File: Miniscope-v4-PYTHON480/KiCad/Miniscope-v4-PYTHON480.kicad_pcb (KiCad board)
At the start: 6 copper layers, 10.5 x 9 mm, 32 parts, among them J1 Conn_01x20, J2 Conn_01x14, Q1 MMBT3904LP-7B, U1 LMV321IDCKR, U2 NOIP1SN0480A, U3 SiT_2.5mmx2mm

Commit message: Not sure why these files changed. Should be just minor stuff
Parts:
- moved L1 0.28 mm to (41.9, 29.4)
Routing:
- net /DOUT5: track 3.86 -> 4.43 mm
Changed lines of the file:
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@@
     (thickness 0.7874)
     (drawings 4)
-    (tracks 429)
+    (tracks 431)
     (zones 0)
     (modules 32)
@@
   )
   (module .Inductor:L_0603_1608Metric_L (layer F.Cu)
-    (at 42.133 29.436 180)
+    (at 41.8536 29.436 180)
     (descr "Inductor, Chip; 1.60 mm L X 0.80 mm W X 1.00 mm H body")
     (attr smd)
@@
   (segment (start 36.1132 28.293) (end 35.569999 28.836201) (width 0.3048) (layer B.Cu) (net 3))
   (via (at 34.9194 31.468) (size 0.3556) (drill 0.1016) (layers F.Cu B.Cu) (net 4))
-  (segment (start 39.4836 30.5884) (end 39.744299 30.327701) (width 0.0762) (layer B.Cu) (net 4))
-  (via (at 39.6946 29.69) (size 0.3556) (drill 0.1016) (layers F.Cu B.Cu) (net 4))
-  (segment (start 39.744299 30.327701) (end 39.744299 29.739699) (width 0.0762) (layer B.Cu) (net 4))
-  (segment (start 39.744299 29.739699) (end 39.6946 29.69) (width 0.0762) (layer B.Cu) (net 4))
-  (segment (start 39.509 29.8756) (end 39.509 30.562) (width 0.0762) (layer F.Cu) (net 4))
-  (segment (start 39.6946 29.69) (end 39.509 29.8756) (width 0.0762) (layer F.Cu) (net 4))
   (segment (start 40.99 29.3598) (end 41.0916 29.436) (width 0.0762) (layer F.Cu) (net 4))
   (via (at 36.570374 31.595) (size 0.3556) (drill 0.1016) (layers F.Cu B.Cu) (net 4))
@@
   (segment (start 36.8708 31.1194) (end 36.570374 31.419826) (width 0.0762) (layer F.Cu) (net 4))
   (segment (start 36.8708 31.1044) (end 36.8708 31.1194) (width 0.0762) (layer F.Cu) (net 4))
-  (segment (start 39.6946 29.438553) (end 39.6946 29.69) (width 0.3048) (layer F.Cu) (net 4))
-  (segment (start 39.951152 29.182001) (end 39.6946 29.438553) (width 0.3048) (layer F.Cu) (net 4))
-  (segment (start 40.812201 29.182001) (end 39.951152 29.182001) (width 0.3048) (layer F.Cu) (net 4))
-  (segment (start 40.99 29.3598) (end 40.812201 29.182001) (width 0.3048) (layer F.Cu) (net 4))
-  (segment (start 36.595786 31.569588) (end 36.570374 31.595) (width 0.3048) (layer In3.Cu) (net 4))
-  (segment (start 36.595786 31.399927) (end 36.595786 31.569588) (width 0.3048) (layer In3.Cu) (net 4))
-  (segment (start 39.6692 29.69) (end 39.643801 29.715399) (width 0.3048) (layer In3.Cu) (net 4))
-  (segment (start 39.6946 29.69) (end 39.6692 29.69) (width 0.3048) (layer In3.Cu) (net 4))
-  (segment (start 39.643801 29.715399) (end 39.643801 29.910473) (width 0.3048) (layer In3.Cu) (net 4))
-  (segment (start 39.643801 29.910473) (end 38.365675 31.188599) (width 0.3048) (layer In3.Cu) (net 4))
-  (segment (start 38.365675 31.188599) (end 36.807114 31.188599) (width 0.3048) (layer In3.Cu) (net 4))
-  (segment (start 36.807114 31.188599) (end 36.595786 31.399927) (width 0.3048) (layer In3.Cu) (net 4))
   (via (at 41.0916 29.436) (size 0.3556) (drill 0.1016) (layers F.Cu B.Cu) (net 4))
   (segment (start 41.244299 29.588699) (end 41.0916 29.436) (width 0.0762) (layer B.Cu) (net 4))
@@
   (segment (start 36.570374 31.595) (end 36.570374 31.7139) (width 0.3048) (layer In3.Cu) (net 4))
   (segment (start 36.570374 31.7139) (end 36.282873 32.001401) (width 0.3048) (layer In3.Cu) (net 4))
+  (via (at 39.69149 29.69) (size 0.3556) (drill 0.1016) (layers F.Cu B.Cu) (net 4))
+  (segment (start 39.509 29.87249) (end 39.513691 29.867799) (width 0.0762) (layer F.Cu) (net 4))
+  (segment (start 36.570374 31.343553) (end 36.725328 31.188599) (width 0.3048) (layer In3.Cu) (net 4))
+  (segment (start 39.4836 30.5884) (end 39.744299 30.327701) (width 0.0762) (layer B.Cu) (net 4))
+  (segment (start 39.744299 30.327701) (end 39.744299 29.994256) (width 0.0762) (layer B.Cu) (net 4))
+  (segment (start 39.69149 29.941447) (end 39.69149 29.69) (width 0.0762) (layer B.Cu) (net 4))
+  (segment (start 36.725328 31.188599) (end 38.444338 31.188599) (width 0.3048) (layer In3.Cu) (net 4))
+  (segment (start 38.444338 31.188599) (end 39.69149 29.941447) (width 0.3048) (layer In3.Cu) (net 4))
+  (segment (start 39.513691 29.867799) (end 39.69149 29.69) (width 0.0762) (layer F.Cu) (net 4))
+  (segment (start 39.744299 29.994256) (end 39.69149 29.941447) (width 0.0762) (layer B.Cu) (net 4))
+  (segment (start 36.570374 31.595) (end 36.570374 31.343553) (width 0.3048) (layer In3.Cu) (net 4))
+  (segment (start 39.509 30.562) (end 39.509 29.87249) (width 0.0762) (layer F.Cu) (net 4))
+  (segment (start 39.69149 29.941447) (end 39.69149 29.69) (width 0.3048) (layer In3.Cu) (net 4))
+  (segment (start 40.5328 28.9026) (end 39.960918 28.9026) (width 0.3048) (layer F.Cu) (net 4))
+  (segment (start 39.682076 29.680586) (end 39.69149 29.69) (width 0.3048) (layer F.Cu) (net 4))
+  (segment (start 40.99 29.3598) (end 40.5328 28.9026) (width 0.3048) (layer F.Cu) (net 4))
+  (segment (start 39.960918 28.9026) (end 39.682076 29.181442) (width 0.3048) (layer F.Cu) (net 4))
+  (segment (start 39.682076 29.181442) (end 39.682076 29.680586) (width 0.3048) (layer F.Cu) (net 4))
   (via (at 35.0464 30.7822) (size 0.3556) (drill 0.1016) (layers F.Cu B.Cu) (net 5))
   (via (at 44.2158 30.8076) (size 0.3556) (drill 0.1016) (layers F.Cu B.Cu) (net 5))
@@
   (segment (start 39.4836 30.0884) (end 39.244299 30.327701) (width 0.0762) (layer B.Cu) (net 41))
   (segment (start 39.244299 30.327701) (end 39.244299 31.308701) (width 0.0762) (layer B.Cu) (net 41))
-  (via (at 40.1772 29.6646) (size 0.3556) (drill 0.1016) (layers F.Cu B.Cu) (net 42))
-  (segment (start 39.9836 30.0884) (end 39.9836 29.8582) (width 0.0762) (layer B.Cu) (net 42))
-  (segment (start 39.9836 29.8582) (end 40.1772 29.6646) (width 0.0762) (layer B.Cu) (net 42))
-  (segment (start 40.1772 29.6646) (end 40.1772 33.0174) (width 0.0762) (layer F.Cu) (net 42))
+  (segment (start 40.088478 32.928678) (end 40.088478 29.627963) (width 0.0762) (layer F.Cu) (net 42))
+  (via (at 40.088478 29.376516) (size 0.3556) (drill 0.1016) (layers F.Cu B.Cu) (net 42))
+  (segment (start 39.9836 29.481394) (end 40.088478 29.376516) (width 0.0762) (layer B.Cu) (net 42))
+  (segment (start 40.088478 29.627963) (end 40.088478 29.376516) (width 0.0762) (layer F.Cu) (net 42))
+  (segment (start 39.9836 30.0884) (end 39.9836 29.481394) (width 0.0762) (layer B.Cu) (net 42))
+  (segment (start 40.1772 33.0174) (end 40.088478 32.928678) (width 0.0762) (layer F.Cu) (net 42))
   (via (at 41.625 32.40781) (size 0.3556) (drill 0.1016) (layers F.Cu B.Cu) (net 43))
   (segment (start 41.625 32.130953) (end 41.625 32.156363) (width 0.0762) (layer B.Cu) (net 43))
@@
   (segment (start 40.4836 30.0884) (end 40.744299 30.349099) (width 0.0762) (layer B.Cu) (net 43))
   (segment (start 41.625 32.156363) (end 41.625 32.40781) (width 0.0762) (layer B.Cu) (net 43))
-  (via (at 40.677211 29.666052) (size 0.3556) (drill 0.1016) (layers F.Cu B.Cu) (net 44))
-  (segment (start 40.9836 30.0884) (end 40.9836 29.972441) (width 0.0762) (layer B.Cu) (net 44))
-  (segment (start 40.9836 29.972441) (end 40.677211 29.666052) (width 0.0762) (layer B.Cu) (net 44))
-  (segment (start 42.103202 32.64079) (end 42.103202 33) (width 0.0762) (layer F.Cu) (net 44))
-  (segment (start 42.103202 32.327913) (end 42.103202 32.64079) (width 0.0762) (layer F.Cu) (net 44))
-  (segment (start 40.677211 30.901922) (end 42.103202 32.327913) (width 0.0762) (layer F.Cu) (net 44))
-  (segment (start 40.677211 29.666052) (end 40.677211 30.901922) (width 0.0762) (layer F.Cu) (net 44))
+  (segment (start 40.9836 30.0884) (end 40.559806 29.664606) (width 0.0762) (layer B.Cu) (net 44))
+  (segment (start 42.103202 32.327913) (end 40.4312 30.655911) (width 0.0762) (layer F.Cu) (net 44))
+  (segment (start 40.559806 29.664606) (end 40.4312 29.664606) (width 0.0762) (layer B.Cu) (net 44))
+  (segment (start 42.103202 33) (end 42.103202 32.327913) (width 0.0762) (layer F.Cu) (net 44))
+  (segment (start 40.4312 29.916053) (end 40.4312 29.664606) (width 0.0762) (layer F.Cu) (net 44))
+  (segment (start 40.4312 30.655911) (end 40.4312 29.916053) (width 0.0762) (layer F.Cu) (net 44))
+  (via (at 40.4312 29.664606) (size 0.3556) (drill 0.1016) (layers F.Cu B.Cu) (net 44))
   (via (at 44.2412 26.9468) (size 0.3556) (drill 0.1016) (layers F.Cu B.Cu) (net 47))
   (segment (start 38.222901 27.827701) (end 38.222901 27.329301) (width 0.0762) (layer B.Cu) (net 47))

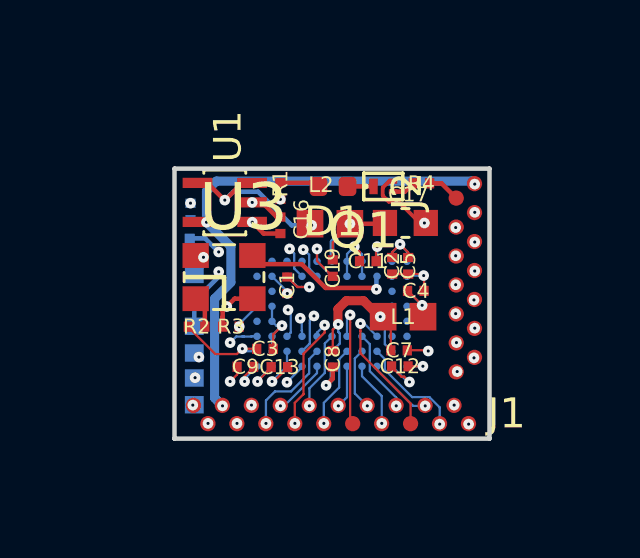
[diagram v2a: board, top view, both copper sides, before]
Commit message: Finalize LED-EWL, MCU, and PYTHON480 PCB for fabrication
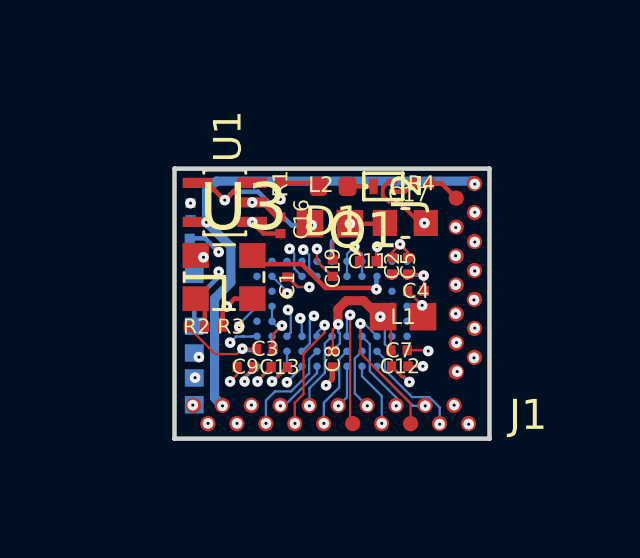
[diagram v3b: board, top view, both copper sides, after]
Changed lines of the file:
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@@
       (outputformat 1)
       (mirror false)
-      (drillshape 1)
+      (drillshape 0)
       (scaleselection 1)
-      (outputdirectory ""))
+      (outputdirectory "Output/"))
   )
   (net 0 "")
@@
   (module .Connector:B2B_Flex_20_Dual_Row_38milx24mil_Pad_20mil (layer F.Cu)
     (at 44.0336 33 180)
-    (fp_text reference J1 (at -1.2664 0.3384 180) (layer F.SilkS)
+    (fp_text reference J1 (at -1.9856 0.2874 180) (layer F.SilkS)
       (effects (font (size 1 1) (thickness 0.15)))
     )

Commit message: Add final gerbers and double check layout for fabrication submitted on 05/03/2019
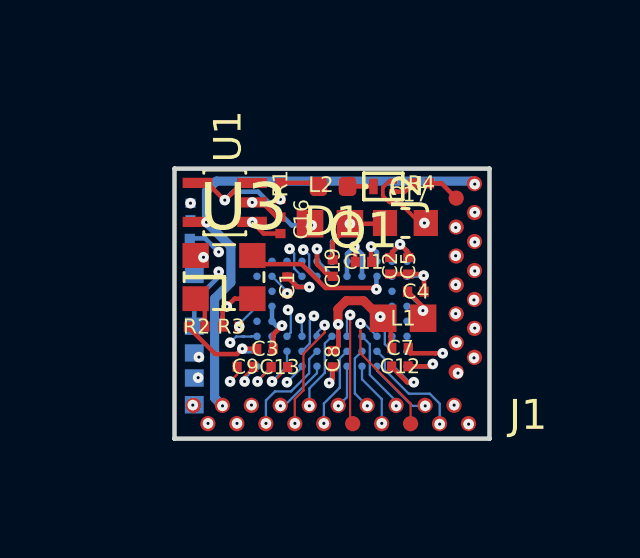
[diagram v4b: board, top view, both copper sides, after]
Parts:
- moved C11 0.15 mm to (40.5, 27.6)
- moved C7 0.09 mm to (41.8, 30.5)
- moved C2 0.07 mm to (41.4, 27.7)
- moved L1 0.05 mm to (41.9, 29.5)
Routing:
- net GND: track 25.0 -> 25.8 mm
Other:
- rule solder_mask_min_width: 0.25 -> 0.1016

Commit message: Finalize routing for Ser-Pow PCB
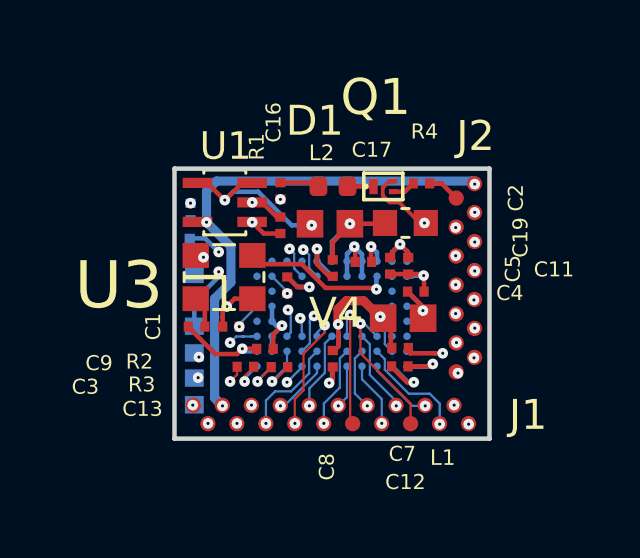
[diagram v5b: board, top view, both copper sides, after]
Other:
- board text added: "V4"
